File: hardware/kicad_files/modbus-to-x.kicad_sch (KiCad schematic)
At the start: 63 parts, among them IC1 ESP32-WROOM-32D_M113DH2800PH3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, J1 PWR, J2 UART, J3 Screw_Terminal_3.5mm_2, J4 SSQ-110-X-X-D, SW1 1825910-7, SW2 1825910-7, U1 AMS1117-3.3, U3 MAX3485, U5 AT24CS64-XHM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

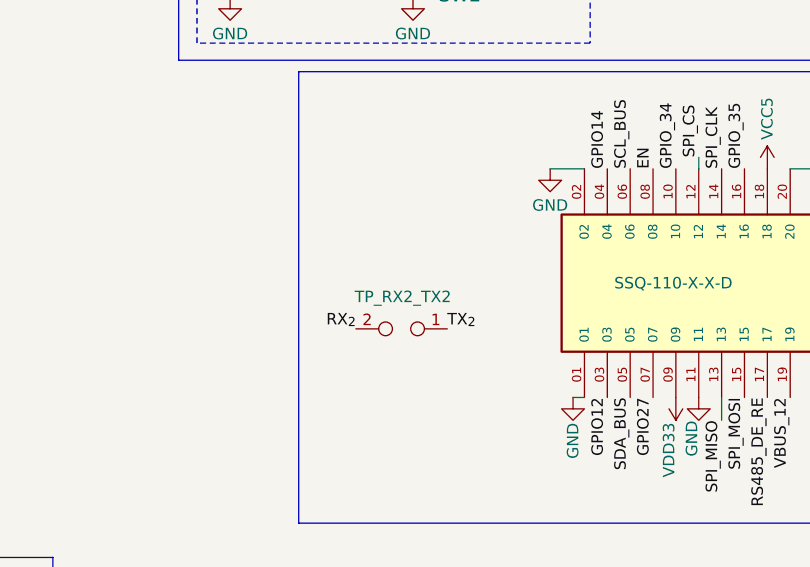
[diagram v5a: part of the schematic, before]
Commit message: added custom symbols
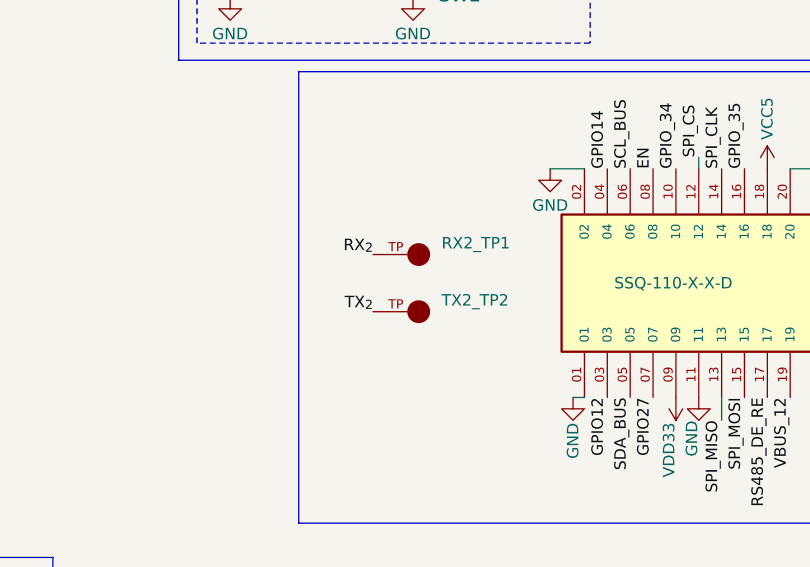
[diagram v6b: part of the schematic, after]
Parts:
- removed TP_RX2_TX2: TestPoint_2Pole, Connector_PinHeader_2.54mm:PinHeader_1x02_P2.54mm_Vertical, symbol Connector:TestPoint_2Pole
- added RX2_TP1, TX2_TP2: 5029, project_footprints:KEYSTONE_5029, symbol KEYSTONE_5029:5029
- C10, C19: footprint Capacitor_SMD:C_0402_1005Metric_Pad0.74x0.62mm_HandSolder -> project_footprints:C_0402_1005Metric_Pad0.74x0.62mm_HandSolder_Modified_Silkscreen
- IC1: footprint footprint_lib:ESP32-WROOM-32D_M113DH2800PH3Q0 -> project_footprints:ESP32-WROOM-32D_M113DH2800PH3Q0
- U7: footprint footprint_lib:LMR14020QDPRRQ1_DPR0010A_Modified_3mm_thermals -> project_footprints:LMR14020QDPRRQ1_DPR0010A_Modified_3mm_thermals
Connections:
- net RX_{2}: now also RX2_TP1.TP
- net TX_{2}: now also TX2_TP2.TP
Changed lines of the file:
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@@
 	)
 	(label "TX_{2}"
-		(at 219.71 143.51 0)
+		(at 211.455 141.605 180)
 		(fields_autoplaced yes)
 		(effects
@@
 				(size 1.27 1.27)
 			)
-			(justify left bottom)
+			(justify right bottom)
 		)
 	)
@@
 	)
 	(label "RX_{2}"
-		(at 209.55 143.51 180)
+		(at 211.455 135.255 180)
 		(fields_autoplaced yes)
 		(effects
@@
 			)
 		)
-		(property "Footprint" "footprint_lib:LMR14020QDPRRQ1_DPR0010A_Modified_3mm_thermals"
+		(property "Footprint" "project_footprints:LMR14020QDPRRQ1_DPR0010A_Modified_3mm_thermals"
 			(at 76.2 40.64 0)
 			(effects
@@
 			)
 		)
-		(property "Footprint" "footprint_lib:ESP32-WROOM-32D_M113DH2800PH3Q0"
+		(property "Footprint" "project_footprints:ESP32-WROOM-32D_M113DH2800PH3Q0"
 			(at 266.7 121.59 0)
 			(effects
@@
 			)
 		)
-		(property "Footprint" "Capacitor_SMD:C_0402_1005Metric_Pad0.74x0.62mm_HandSolder"
+		(property "Footprint" "project_footprints:C_0402_1005Metric_Pad0.74x0.62mm_HandSolder_Modified_Silkscreen"
 			(at 54.9148 20.32 0)
 			(effects
@@
 	)
 	(symbol
+		(lib_id "KEYSTONE_5029:5029")
+		(at 216.535 141.605 0)
+		(unit 1)
+		(exclude_from_sim no)
+		(in_bom yes)
+		(on_board yes)
+		(dnp no)
+		(fields_autoplaced yes)
+		(property "Reference" "TX2_TP2"
+			(at 219.075 140.3349 0)
+			(effects
+				(font
+					(size 1.27 1.27)
+				)
+				(justify left)
+			)
+		)
+		(property "Value" "5029"
+			(at 219.075 142.8749 0)
+			(effects
+				(font
+					(size 1.27 1.27)
+				)
+				(justify left)
+				(hide yes)
+			)
+		)
+		(property "Footprint" "project_footprints:KEYSTONE_5029"
+			(at 216.535 141.605 0)
+			(effects
+				(font
+					(size 1.27 1.27)
+				)
+				(justify bottom)
+				(hide yes)
+			)
+		)
+		(property "Datasheet" "https://www.keyelco.com/product-pdf.cfm?p=1358"
+			(at 216.535 141.605 0)
+			(effects
+				(font
+					(size 1.27 1.27)
+				)
+				(hide yes)
+			)
+		)
+		(property "Description" "PC Test Point, Miniature Phosphor Bronze Silver Plating Surface Mount Mounting Type"
+			(at 216.535 141.605 0)
+			(effects
+				(font
+					(size 1.27 1.27)
+				)
+				(hide yes)
+			)
+		)
+		(pin "TP"
+		)
+		(instances
+			(project "modbus-to-x"
+				(path "/d5b026e9-d5a5-415b-84cb-4c68355c0f8f"
+					(reference "TX2_TP2")
+					(unit 1)
+				)
+			)
+		)
+	)
+	(symbol
 		(lib_id "power:GND")
 		(at 77.47 153.67 0)
@@
 	)
 	(symbol
-		(lib_id "Connector:TestPoint_2Pole")
-		(at 214.63 143.51 180)
-		(unit 1)
-		(exclude_from_sim no)
-		(in_bom yes)
-		(on_board yes)
-		(dnp no)
-		(property "Reference" "TP_RX2_TX2"
-			(at 209.423 139.954 0)
-			(effects
-				(font
-					(size 1.27 1.27)
-				)
-				(justify right)
-			)
-		)
-		(property "Value" "TestPoint_2Pole"
-			(at 215.8999 140.97 90)
-			(effects
-				(font
-					(size 1.27 1.27)
-				)
-				(justify right)
-				(hide yes)
-			)
-		)
-		(property "Footprint" "Connector_PinHeader_2.54mm:PinHeader_1x02_P2.54mm_Vertical"
-			(at 214.63 143.51 0)
-			(effects
-				(font
-					(size 1.27 1.27)
-				)
-				(hide yes)
-			)
-		)
-		(property "Datasheet" "~"
-			(at 214.63 143.51 0)
-			(effects
-				(font
-					(size 1.27 1.27)
-				)
-				(hide yes)
-			)
-		)
-		(property "Description" "2-polar test point"
-			(at 214.63 143.51 0)
-			(effects
-				(font
-					(size 1.27 1.27)
-				)
-				(hide yes)
-			)
-		)
-		(pin "2"
-		)
-		(pin "1"
-		)
-		(instances
-			(project ""
-				(path "/d5b026e9-d5a5-415b-84cb-4c68355c0f8f"
-					(reference "TP_RX2_TX2")
-					(unit 1)
-				)
-			)
-		)
-	)
-	(symbol
 		(lib_id "power:GND")
 		(at 41.91 119.38 0)
@@
 	)
 	(symbol
+		(lib_id "KEYSTONE_5029:5029")
+		(at 216.535 135.255 0)
+		(unit 1)
+		(exclude_from_sim no)
+		(in_bom yes)
+		(on_board yes)
+		(dnp no)
+		(fields_autoplaced yes)
+		(property "Reference" "RX2_TP1"
+			(at 219.075 133.9849 0)
+			(effects
+				(font
+					(size 1.27 1.27)
+				)
+				(justify left)
+			)
+		)
+		(property "Value" "5029"
+			(at 219.075 136.5249 0)
+			(effects
+				(font
+					(size 1.27 1.27)
+				)
+				(justify left)
+				(hide yes)
+			)
+		)
+		(property "Footprint" "project_footprints:KEYSTONE_5029"
+			(at 216.535 135.255 0)
+			(effects
+				(font
+					(size 1.27 1.27)
+				)
+				(justify bottom)
+				(hide yes)
+			)
+		)
+		(property "Datasheet" "https://www.keyelco.com/product-pdf.cfm?p=1358"
+			(at 216.535 135.255 0)
+			(effects
+				(font
+					(size 1.27 1.27)
+				)
+				(hide yes)
+			)
+		)
+		(property "Description" "PC Test Point, Miniature Phosphor Bronze Silver Plating Surface Mount Mounting Type"
+			(at 216.535 135.255 0)
+			(effects
+				(font
+					(size 1.27 1.27)
+				)
+				(hide yes)
+			)
+		)
+		(pin "TP"
+		)
+		(instances
+			(project ""
+				(path "/d5b026e9-d5a5-415b-84cb-4c68355c0f8f"
+					(reference "RX2_TP1")
+					(unit 1)
+				)
+			)
+		)
+	)
+	(symbol
 		(lib_id "power:GND")
 		(at 24.13 38.1 0)
@@
 			)
 		)
-		(property "Footprint" "Capacitor_SMD:C_0402_1005Metric_Pad0.74x0.62mm_HandSolder"
+		(property "Footprint" "project_footprints:C_0402_1005Metric_Pad0.74x0.62mm_HandSolder_Modified_Silkscreen"
 			(at 96.52 28.9052 0)
 			(effects

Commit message: wip
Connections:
- net STAT_1 renamed LED_C
- net STAT_2 renamed LED_B
- net STAT_3 renamed LED_A
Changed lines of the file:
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@@
 		)
 	)
-	(label "STAT_1"
+	(label "LED_C"
 		(at 110.49 138.43 90)
 		(fields_autoplaced yes)
@@
 		)
 	)
-	(label "STAT_1"
+	(label "LED_C"
 		(at 232.41 46.99 180)
 		(fields_autoplaced yes)
@@
 		)
 	)
-	(label "STAT_3"
+	(label "LED_A"
 		(at 120.65 138.43 90)
 		(fields_autoplaced yes)
@@
 		)
 	)
-	(label "STAT_3"
+	(label "LED_A"
 		(at 232.41 52.07 180)
 		(fields_autoplaced yes)
@@
 		)
 	)
-	(label "STAT_2"
+	(label "LED_B"
 		(at 232.41 49.53 180)
 		(fields_autoplaced yes)
@@
 		)
 	)
-	(label "STAT_2"
+	(label "LED_B"
 		(at 115.57 138.43 90)
 		(fields_autoplaced yes)

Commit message: revised hw
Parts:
- removed J4: SSQ-110-X-X-D, Connector Receptable 2x10 20POS:SAMTEC_SSQ-110-X-X-D, symbol Connector Receptable 2x10 20POS:SSQ-110-X-X-D
- added FB_NODE_TP3, L1_COUT_TP6, SW_TP4, VCC5_TP5: 5029, project_footprints:KEYSTONE_5029, symbol KEYSTONE_5029:5029
- C10: footprint project_footprints:C_0402_1005Metric_Pad0.74x0.62mm_HandSolder_Modified_Silkscreen -> Capacitor_SMD:C_0805_2012Metric_Pad1.18x1.45mm_HandSolder; PartNo CC0402MRX5R7BB104 -> GCD21BR71H104KA01L; Voltage 16V -> 50V
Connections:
- net VCC5: now also L1_COUT_TP6.TP, VCC5_TP5.TP
- net FB_NODE: now reaches C12.1, C21.1, R10.2, R8.2, U7.7 (FB)
- net FB_NODE: now also FB_NODE_TP3.TP
- net SW_NODE: now reaches C10.1, D2.1 (K), L1.1, U7.10 (SW)
- net SW_NODE: now also SW_TP4.TP
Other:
- moved on the sheet: RX2_TP1, TX2_TP2
